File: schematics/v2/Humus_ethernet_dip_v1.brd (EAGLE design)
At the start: 41 x 50 mm, 31 parts, among them IC2 DS2432P

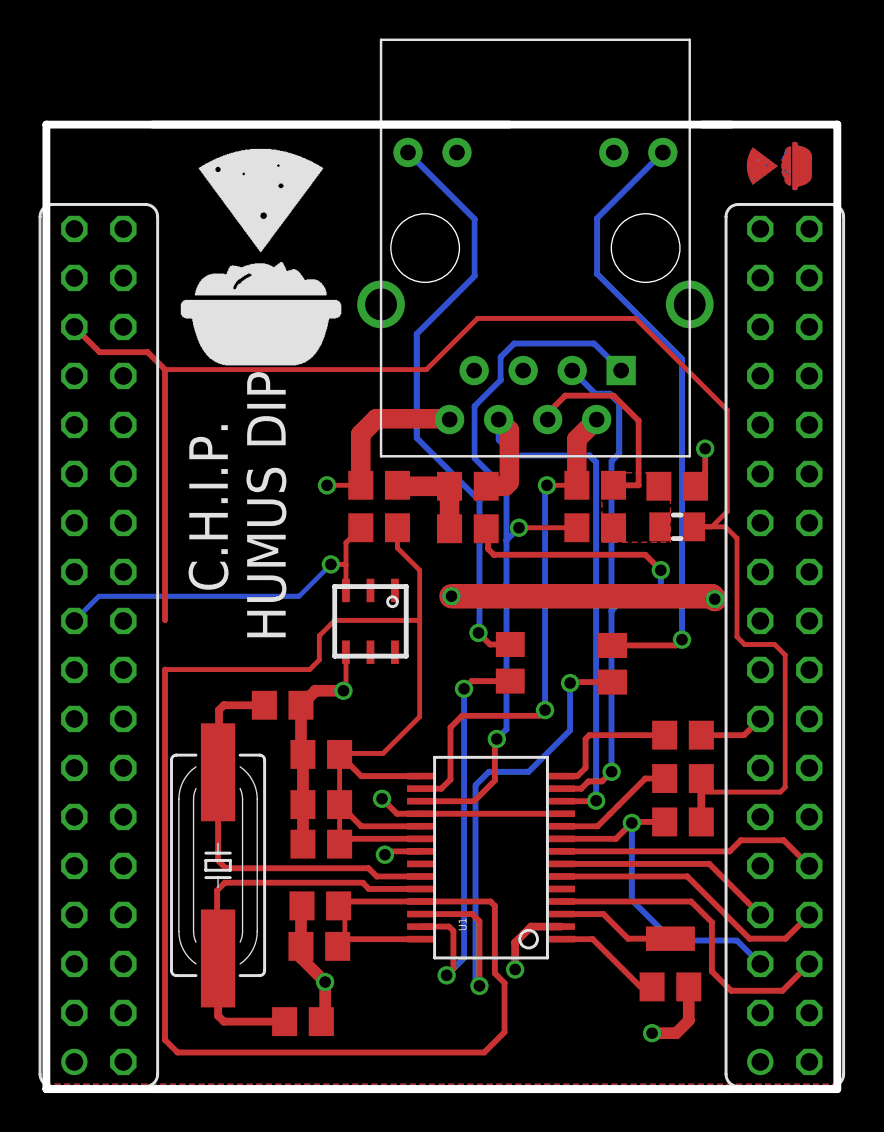
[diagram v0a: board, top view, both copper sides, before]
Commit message: added version two with EEPROM and DCDC
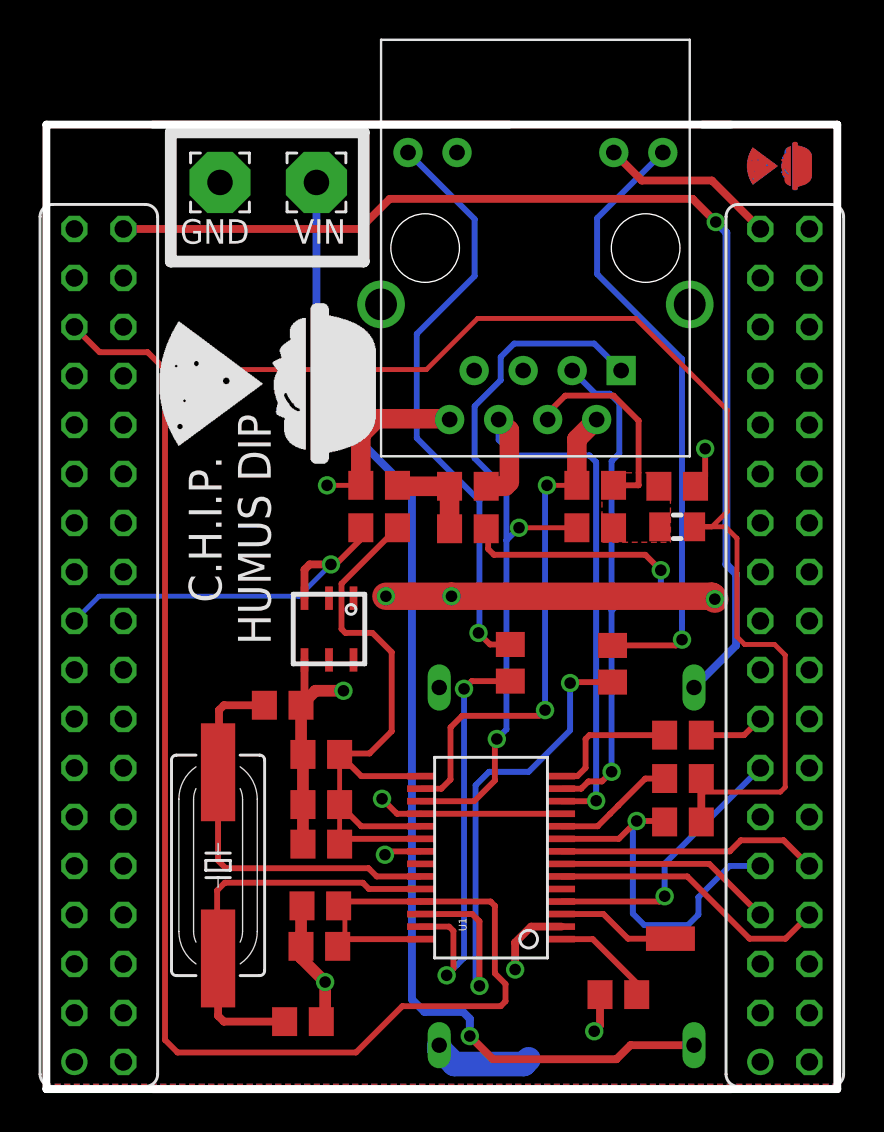
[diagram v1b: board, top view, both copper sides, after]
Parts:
- added GND, VIN: WIREPAD3,17/1,3, wirepad:3,17/1,3
- added U$9: MP1584EN_FRAMELESS, power_supply:MP1584EN_FRAMELESS
- moved U$5 11.4 mm to (17.1, 32.4), turned to 90 degrees
- moved C1 2.73 mm to (29.6, 4.90), turned to 180 degrees
- moved IC2 2.19 mm to (14.7, 23.9)
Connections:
- new net VIN: U$9.VIN, VIN.1
- net AP2: now also U1.4
- net CHR_IN: now also U$9.VOUT
- net CSIPCK: now also R3.1, U1.9
- net D0: no longer R3.1, U1.9
- net D1: no longer U1.4
- net GND: now also GND.1, U$9.GNDIN, U$9.GNDOUT
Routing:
- net VIN: track 0.00 -> 61.1 mm, vias 0 -> 1
- net CHR_IN: track 0.00 -> 57.3 mm, vias 0 -> 1
- net CSIPCK: track 0.00 -> 19.3 mm, vias 0 -> 1
- net D0: track 17.7 -> 0.00 mm, vias 1 -> 0
- net D1: track 16.8 -> 0.00 mm
- net GND: track 66.7 -> 83.2 mm, vias 10 -> 11
- net AP2: track 0.00 -> 14.2 mm, vias 0 -> 1
- net VDD: track 189.4 -> 177.7 mm
- net LD2: track 19.0 -> 20.2 mm
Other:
- board text added: "JKW v0.2"
- board text removed: "JKW v0.1"

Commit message: fixed connection
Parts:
- removed GND, VIN: WIREPAD3,17/1,3, wirepad:3,17/1,3
- removed R3: (no value), rcl:R0805
- removed U$9: MP1584EN_FRAMELESS, power_supply:MP1584EN_FRAMELESS
- moved U$5 11.4 mm to (6.95, 37.5), turned to 0 degrees
- moved C1 2.73 mm to (32.4, 5.30), turned to 0 degrees
- moved IC2 2.19 mm to (16.8, 24.2)
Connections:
- removed net VIN: U$9.VIN, VIN.1
- net CHR_IN: no longer U$9.VOUT
- net CSIPCK: no longer R3.1
- net GND: no longer GND.1, U$9.GNDIN, U$9.GNDOUT
- net VDD: no longer R3.2
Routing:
- net VIN: track 61.1 -> 0.00 mm, vias 1 -> 0
- net CHR_IN: track 57.3 -> 0.00 mm, vias 1 -> 0
- net GND: track 83.2 -> 66.7 mm, vias 11 -> 10
- net VDD: track 177.7 -> 187.7 mm
- net CSIPCK: track 19.3 -> 10.9 mm, vias 1 -> 0
- net AP2: track 14.2 -> 16.0 mm
- net LD2: track 20.2 -> 19.0 mm
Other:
- board text added: "JKW v0.1"
- board text removed: "JKW v0.2"
